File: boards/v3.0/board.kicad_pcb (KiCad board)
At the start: 2 copper layers, 65 parts, among them J2 KF301-2P, J3 KF301-2P, J4 KF301-2P, J5 KF301-2P, J6 KF301-2P, J7 KF301-2P, P1 Pin Header, P2 Pin Header, P3 Pin Header, P4 Pin Header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

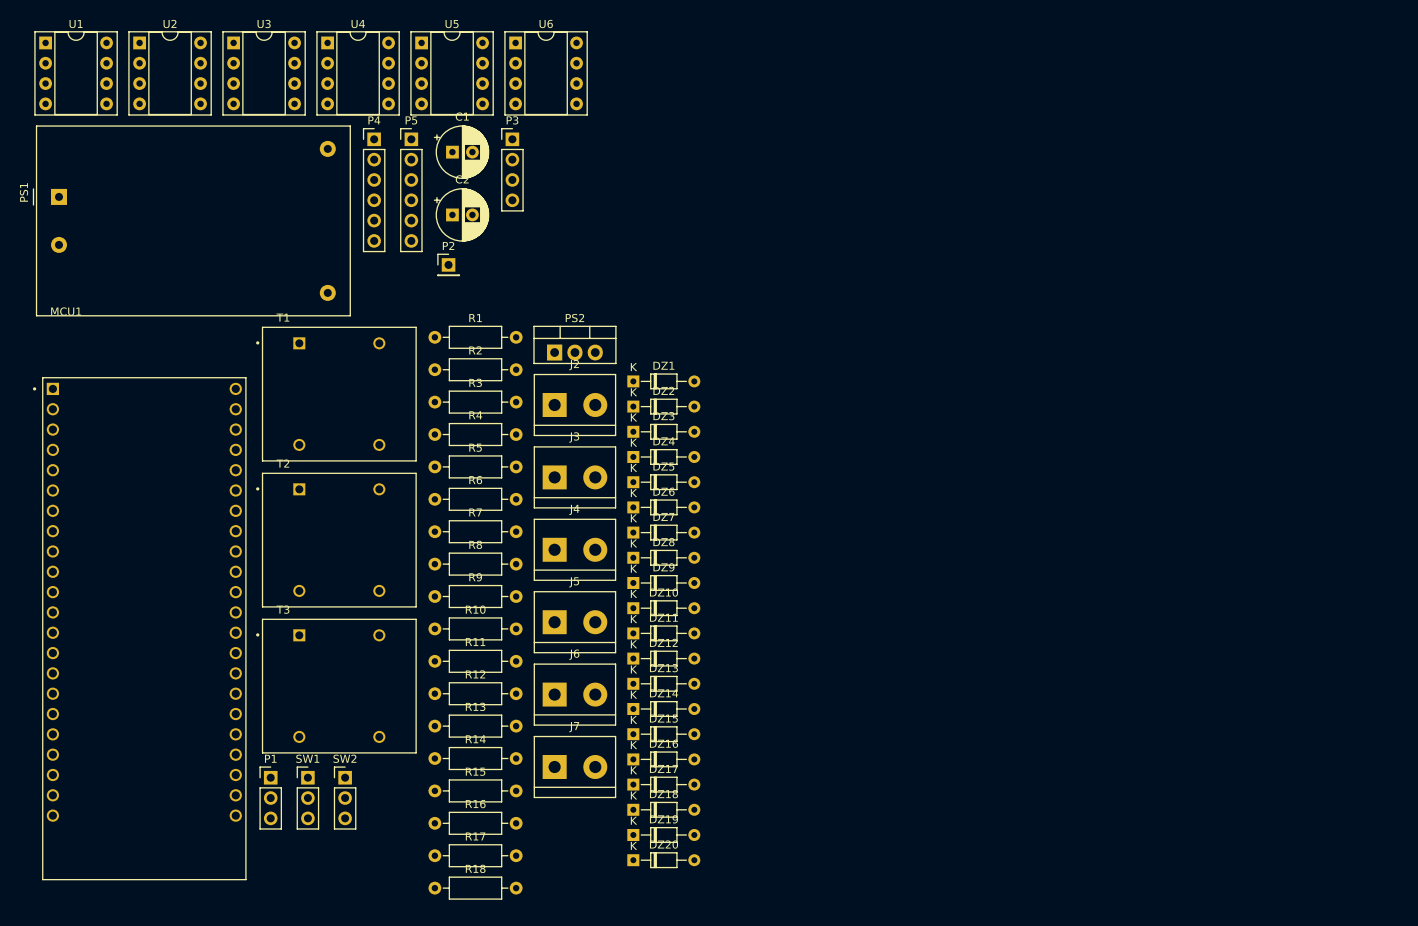
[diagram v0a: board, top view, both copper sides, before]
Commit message: Finish of board v3.0 development and code update
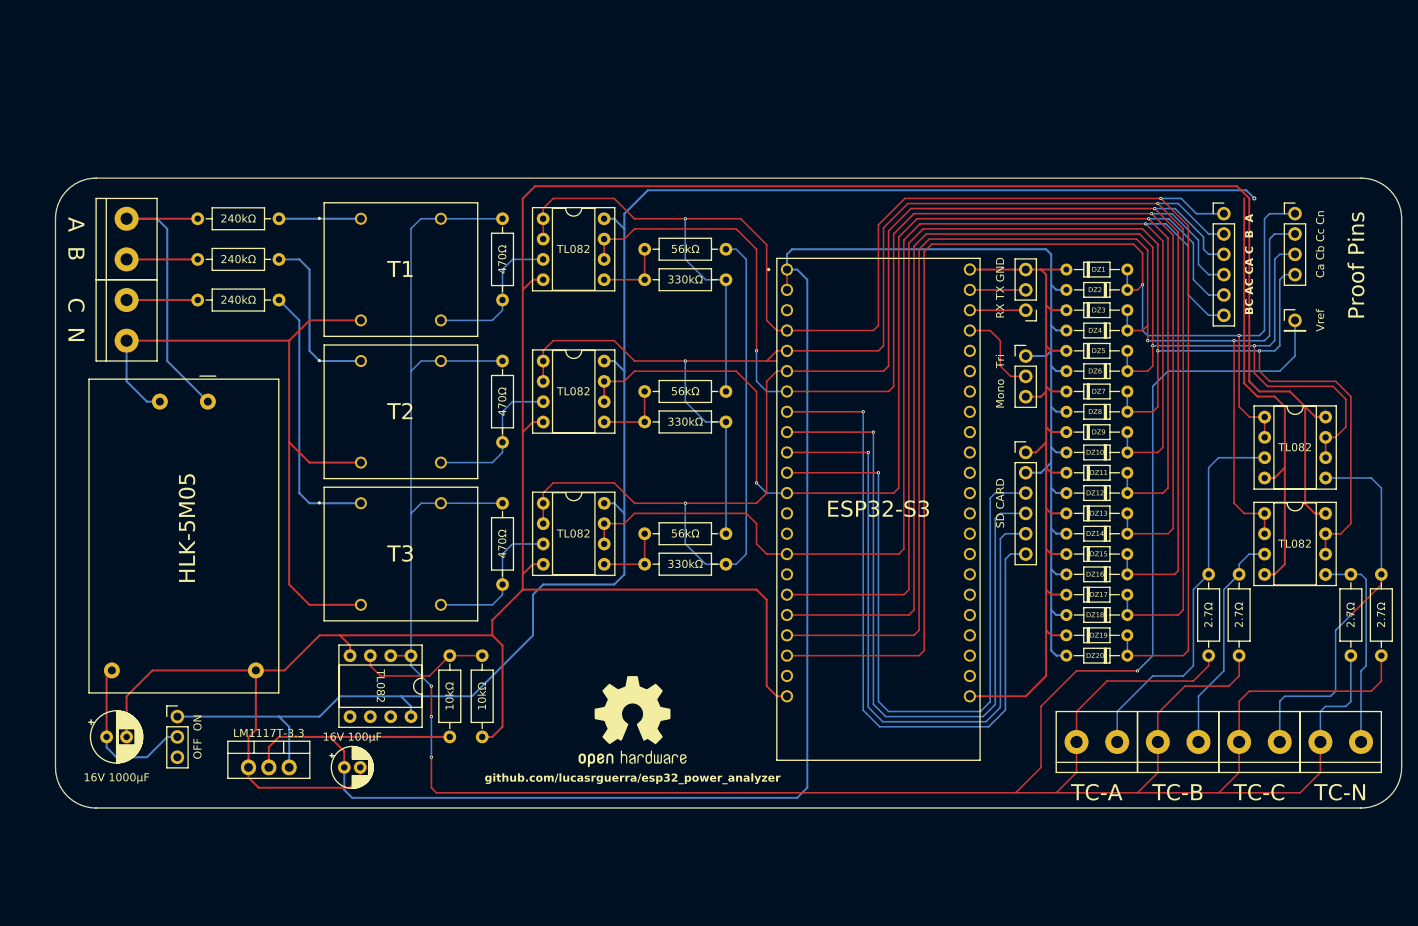
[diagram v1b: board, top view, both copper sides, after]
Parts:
- removed J7: KF301-2P, TerminalBlock:TerminalBlock_bornier-2_P5.08mm
- added G***: LOGO, LOGO, F.Cu at (135.6, 117.5)
- added J1: KF301-2P, TerminalBlock:TerminalBlock_bornier-2_P5.08mm, F.Cu at (72.4, 54.6)
- C2: value 25V 220µF -> 16V 100µF; footprint Capacitor_THT:CP_Radial_D6.3mm_P2.50mm -> Capacitor_THT:CP_Radial_D5.0mm_P2.00mm
- moved R17 123.4 mm to (229.2, 99.1), turned to -90 degrees
- moved R18 121.0 mm to (225.4, 99.1), turned to -90 degrees
- moved U5 115.3 mm to (214.7, 79.4)
- moved P1 111.0 mm to (184.8, 66.0), turned to 180 degrees
- moved U6 110.6 mm to (214.6, 91.5)
- moved P4 106.6 mm to (209.6, 54.0)
- moved P2 106.0 mm to (218.4, 67.3)
- moved R16 105.2 mm to (211.5, 99.1), turned to -90 degrees
- moved R15 100.4 mm to (207.6, 99.1), turned to -90 degrees
- moved SW2 100.1 mm to (184.8, 71.8)
- moved P3 98.3 mm to (218.4, 54.0)
- moved J6 95.9 mm to (221.6, 120.0)
- moved MCU1 93.0 mm to (166.4, 90.9)
- moved U1 89.2 mm to (107.9, 109.2), turned to -90 degrees
- moved J5 86.9 mm to (211.5, 120.0)
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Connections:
- C1 pad 1: Vin -> Power
- DZ1 pad 2: Treated Wave A -> Current A
- DZ10 pad 1: Treated Wave AB -> Treated Wave BC
- DZ11 pad 2: Treated Wave BC -> Treated Wave AB
- DZ12 pad 1: Treated Wave BC -> Treated Wave AB
- DZ13 pad 2: Current A -> Treated Wave CA
- DZ14 pad 1: Current A -> Treated Wave CA
- DZ15 pad 2: Current B -> Treated Wave C
- DZ16 pad 1: Current B -> Treated Wave C
- DZ17 pad 2: Current C -> Treated Wave B
- DZ18 pad 1: Current C -> Treated Wave B
- DZ19 pad 2: Current N -> Treated Wave A
- DZ2 pad 1: Treated Wave A -> Current A
- DZ20 pad 1: Current N -> Treated Wave A
- DZ3 pad 2: Treated Wave B -> Current B
- DZ4 pad 1: Treated Wave B -> Current B
- DZ5 pad 2: Treated Wave C -> Current C
- DZ6 pad 1: Treated Wave C -> Current C
- DZ7 pad 2: Treated Wave CA -> Current N
- DZ8 pad 1: Treated Wave CA -> Current N
- DZ9 pad 2: Treated Wave AB -> Treated Wave BC
- J3 pad 1: Line A -> TC A-2
- J3 pad 2: Line B -> TC A-1
- J4 pad 2: TC A-1 -> TC B-1
- J5 pad 2: TC B-1 -> TC C-1
- J6 pad 2: TC C-1 -> TC N-1
- P4 pad 1: Treated Wave C -> Treated Wave A
- P4 pad 3: Treated Wave A -> Treated Wave C
- P4 pad 4: Treated Wave BC -> Treated Wave CA
- P4 pad 6: Treated Wave CA -> Treated Wave BC
- PS1 pad 4: Vin -> Power
- PS2 pad 3: Net-(PS2-VI) -> Vin
- SW1 pad 1: Net-(PS2-VI) -> Vin
- SW1 pad 2: Vin -> Power
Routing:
- net GND: track 0.00 -> 464.5 mm
- net TC A-2: track 0.00 -> 417.1 mm, vias 0 -> 4
- net Vcc: track 0.00 -> 274.8 mm
- net Vin: track 0.00 -> 260.2 mm, vias 0 -> 1
- net Treated Wave C: track 0.00 -> 236.8 mm, vias 0 -> 2
- net Treated Wave A: track 0.00 -> 210.3 mm, vias 0 -> 2
- net Treated Wave B: track 0.00 -> 197.2 mm, vias 0 -> 2
- net Current N: track 0.00 -> 181.7 mm, vias 0 -> 2
- net Treated Wave AB: track 0.00 -> 175.3 mm, vias 0 -> 2
- net Treated Wave CA: track 0.00 -> 172.9 mm, vias 0 -> 2
- net Current B: track 0.00 -> 168.9 mm, vias 0 -> 2
- net Treated Wave BC: track 0.00 -> 168.2 mm, vias 0 -> 1
- net Current C: track 0.00 -> 167.3 mm, vias 0 -> 2
- net Current A: track 0.00 -> 158.8 mm, vias 0 -> 2
- net Neutral: track 0.00 -> 91.2 mm
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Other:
- board outline added: 168.3 x 78.7 mm
- board text added: "Proof Pins"
- board text added: "github.com/lucasrguerra/esp32_power_analyzer"

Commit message: Revision of the v3.0 board
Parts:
- moved J6 141.3 mm to (102.2, 44.5), turned to 180 degrees
- moved R18 129.1 mm to (102.2, 60.3), turned to 90 degrees
- moved J5 124.6 mm to (112.4, 44.5), turned to 180 degrees
- moved R17 123.1 mm to (112.4, 60.3), turned to 90 degrees
- moved J4 109.1 mm to (122.6, 44.5), turned to 180 degrees
- moved R16 97.0 mm to (122.6, 60.3), turned to 90 degrees
- moved J3 95.5 mm to (132.7, 44.5), turned to 180 degrees
- moved R15 84.3 mm to (132.7, 60.3), turned to 90 degrees
- moved DZ20 69.2 mm to (148.6, 60.3), turned to 90 degrees
- moved U5 67.7 mm to (160.0, 39.4), turned to -90 degrees
- moved DZ19 66.4 mm to (151.1, 52.7), turned to -90 degrees
- moved U6 64.2 mm to (177.2, 39.4), turned to -90 degrees
- moved DZ18 62.0 mm to (153.7, 60.3), turned to 90 degrees
- moved DZ17 59.4 mm to (156.2, 52.7), turned to -90 degrees
- moved DZ16 54.8 mm to (158.8, 60.3), turned to 90 degrees
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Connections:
- R15 pad 1: TC A-1 -> TC B-1
- R16 pad 1: TC B-1 -> TC C-1
- R17 pad 1: TC C-1 -> TC A-1
- U5 pad 1: Current A -> Current B
- U5 pad 2: Current A -> Current B
- U5 pad 3: TC A-1 -> TC B-1
- U6 pad 1: Current B -> Current A
- U6 pad 2: Current B -> Current A
- U6 pad 3: TC B-1 -> TC A-1
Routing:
- net TC A-2: track 417.1 -> 165.7 mm, vias 4 -> 0
- net TC N-1: track 25.9 -> 105.7 mm
- net Treated Wave A: track 210.3 -> 151.5 mm
- net Vin: track 260.2 -> 204.0 mm, vias 1 -> 0
- net GND: track 464.5 -> 411.8 mm, vias 0 -> 1
- net TC B-1: track 28.0 -> 79.2 mm
- net Treated Wave CA: track 172.9 -> 123.9 mm, vias 2 -> 1
- net Treated Wave AB: track 175.3 -> 129.5 mm, vias 2 -> 1
- net Treated Wave B: track 197.2 -> 157.3 mm, vias 2 -> 3
- net Treated Wave C: track 236.8 -> 202.6 mm, vias 2 -> 3
- net Treated Wave BC: track 168.2 -> 134.1 mm
- net TC A-1: track 48.8 -> 82.4 mm
- net Vcc: track 274.8 -> 307.6 mm, vias 0 -> 2
- net TC C-1: track 47.8 -> 76.5 mm, vias 1 -> 0
- net Current N: track 181.7 -> 156.0 mm
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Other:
- board size 168.3 x 78.7 mm -> 121.9 x 105.4 mm
- board text added: "Analisador de Qualidade de Energia"
- board text removed: "Proof Pins"

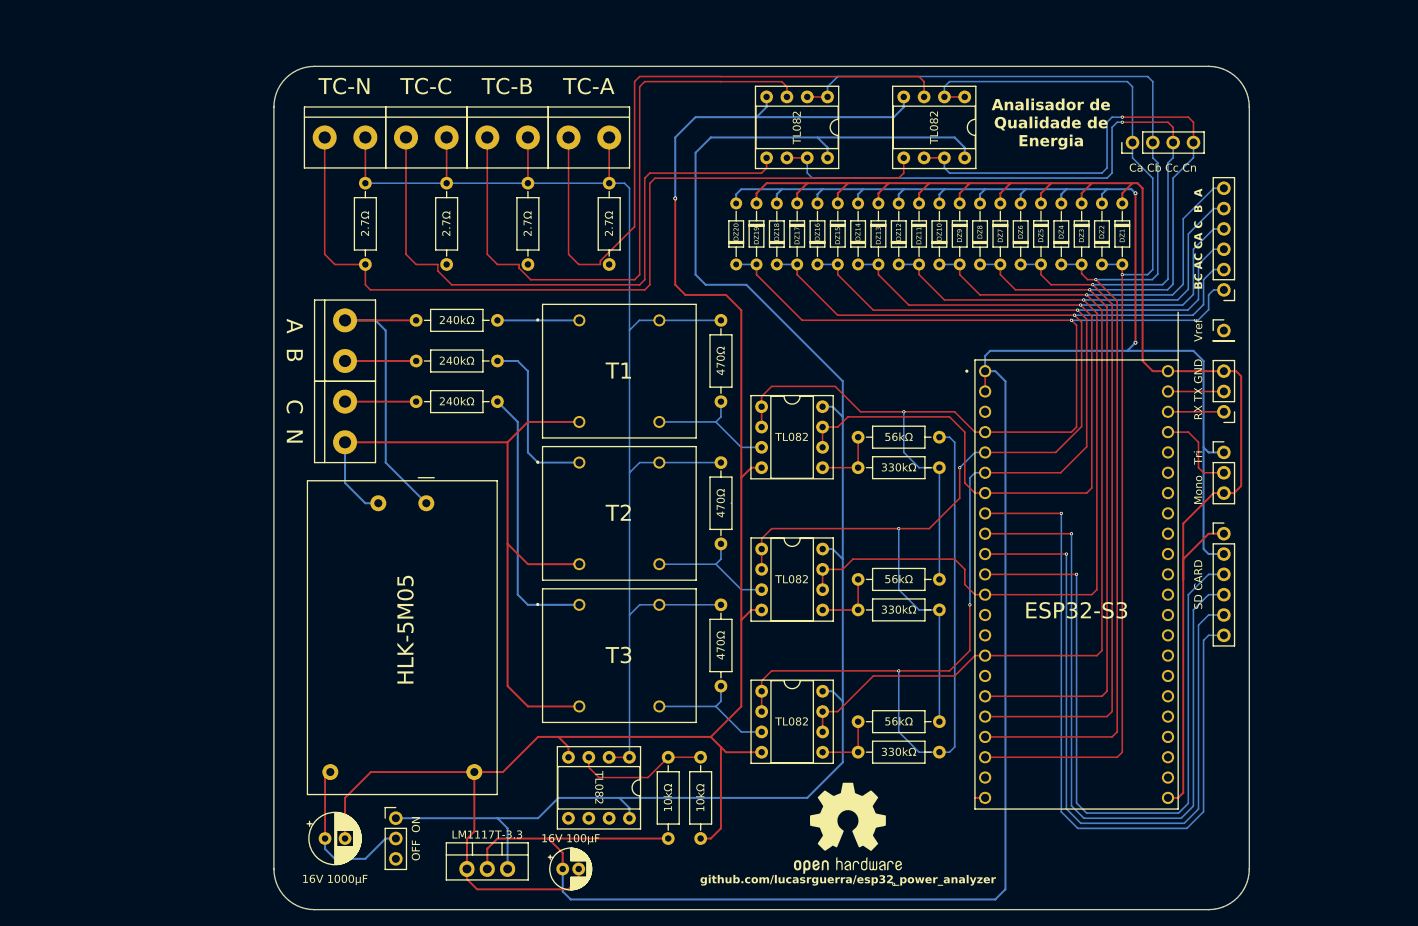
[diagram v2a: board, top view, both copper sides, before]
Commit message: Reduction in the size of v3.0 board
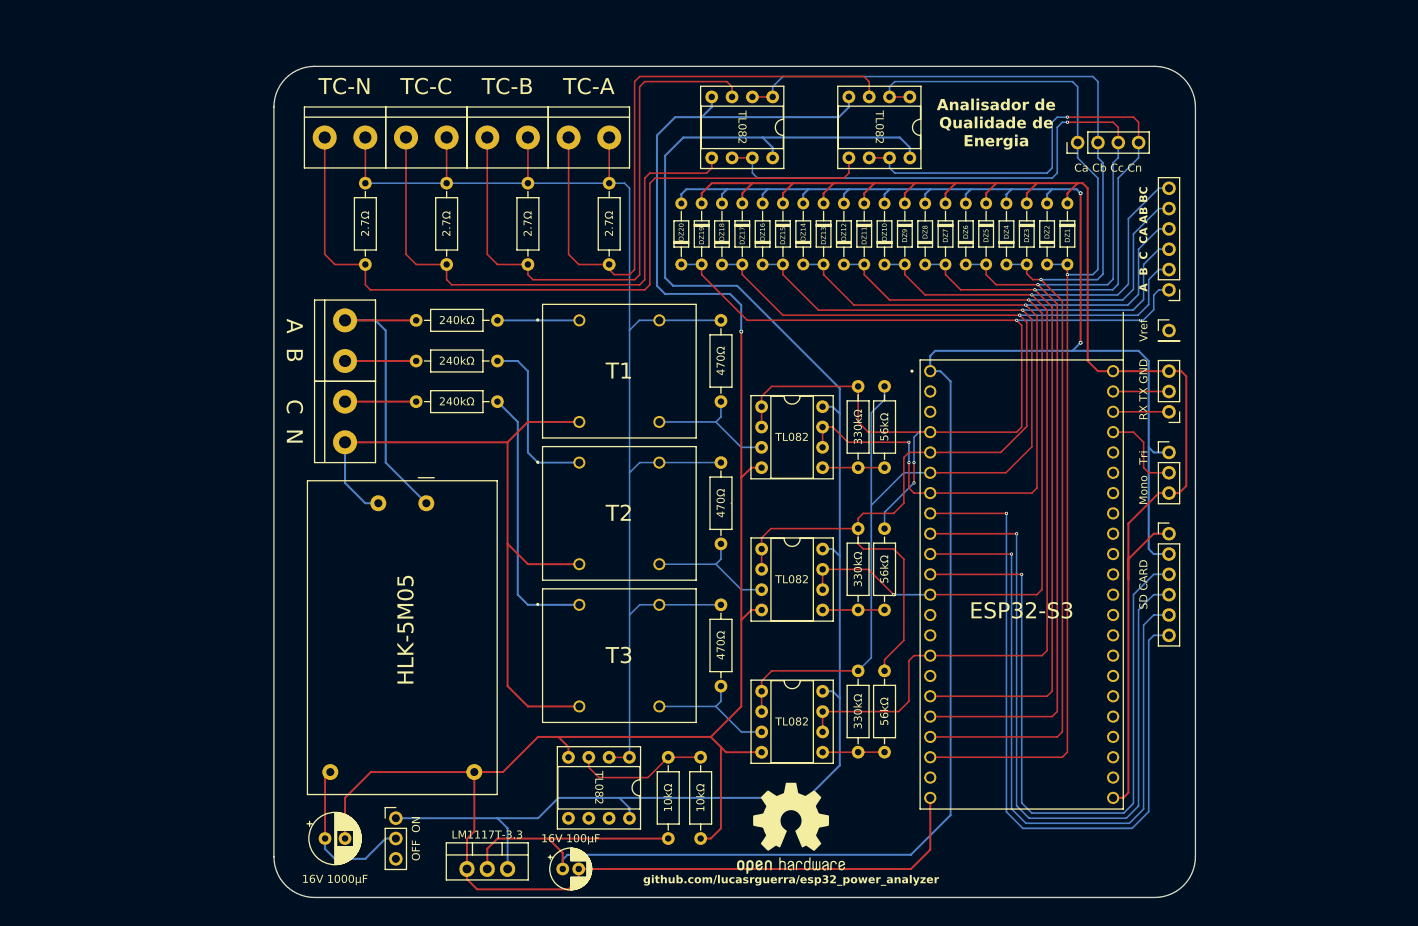
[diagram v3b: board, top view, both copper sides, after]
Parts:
- moved R17 20.3 mm to (132.7, 60.3)
- moved R11 14.4 mm to (163.8, 93.3), turned to -90 degrees
- moved R13 14.4 mm to (163.8, 111.1), turned to -90 degrees
- moved R9 14.4 mm to (163.8, 75.6), turned to -90 degrees
- moved R16 10.2 mm to (112.4, 60.3)
- moved R15 10.2 mm to (122.6, 60.3)
- moved R10 9.35 mm to (167.1, 75.6), turned to -90 degrees
- moved R12 9.35 mm to (167.1, 93.3), turned to -90 degrees
- moved R14 9.35 mm to (167.1, 111.1), turned to -90 degrees
- moved G*** 7.11 mm to (155.4, 130.8)
- moved DZ1 6.86 mm to (190.0, 52.7)
- moved DZ10 6.86 mm to (167.1, 60.3)
- moved DZ12 6.86 mm to (162.1, 60.3)
- moved DZ13 6.86 mm to (159.5, 52.7)
- moved DZ14 6.86 mm to (157.0, 60.3)
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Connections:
- MCU1 pad J1_2: Vcc -> unconnected-(MCU1-3V3__1-PadJ1_2)
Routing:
- net Treated Wave C: track 202.6 -> 153.6 mm, vias 3 -> 1
- net GND: track 411.8 -> 460.3 mm
- net Vcc: track 307.6 -> 288.7 mm
- net Treated Wave A: track 151.5 -> 138.2 mm, vias 2 -> 3
- net Treated Wave B: track 157.3 -> 148.0 mm, vias 3 -> 1
- net Treated Wave AB: track 129.5 -> 120.4 mm, vias 1 -> 2
- net Treated Wave CA: track 123.9 -> 115.6 mm, vias 1 -> 3
- net TC N-1: track 105.7 -> 98.8 mm
- net TC B-1: track 79.2 -> 72.8 mm
- net TC C-1: track 76.5 -> 70.3 mm
- net Treated Wave BC: track 134.1 -> 130.2 mm
- net TC A-1: track 82.4 -> 79.8 mm
- net Vin: track 204.0 -> 202.1 mm
- net Net-(U4B-+): track 8.25 -> 7.74 mm
- net Net-(U3B-+): track 8.25 -> 7.74 mm
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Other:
- board size 121.9 x 105.4 mm -> 115.2 x 103.9 mm

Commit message: Revision in the v3.0 board
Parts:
- moved G*** 90.7 mm to (180.6, 43.7)
- moved PS2 27.4 mm to (139.7, 124.1)
- moved C1 26.7 mm to (123.3, 126.4)
- moved SW1 26.3 mm to (131.4, 122.6)
- moved U1 24.1 mm to (159.4, 121.3)
- moved R1 23.8 mm to (163.8, 130.8)
- moved R2 23.0 mm to (167.1, 120.7)
- moved C2 16.3 mm to (141.7, 129.1), turned to 180 degrees
- moved R10 5.72 mm to (167.1, 69.8)
- moved R11 5.72 mm to (163.8, 87.6)
- moved R12 5.72 mm to (167.1, 87.6)
- moved R13 5.72 mm to (163.8, 105.4)
- moved R14 5.72 mm to (167.1, 105.4)
- moved R9 5.72 mm to (163.8, 69.8)
- moved U2 5.72 mm to (151.8, 72.4)
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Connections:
- MCU1 pad J1_12: Treated Wave AB -> Treated Wave C
- MCU1 pad J1_5: Treated Wave B -> Treated Wave CA
- MCU1 pad J1_6: Treated Wave C -> Treated Wave B
- MCU1 pad J1_7: Treated Wave CA -> Treated Wave AB
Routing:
- net GND: track 460.3 -> 385.7 mm
- net Vcc: track 288.7 -> 251.8 mm
- net TC A-2: track 165.7 -> 188.4 mm
- net Vin: track 202.1 -> 179.7 mm
- net Treated Wave C: track 153.6 -> 173.7 mm
- net Power: track 20.3 -> 38.7 mm
- net Treated Wave AB: track 120.4 -> 108.4 mm, vias 2 -> 3
- net Treated Wave A: track 138.2 -> 142.6 mm, vias 3 -> 1
- net Treated Wave BC: track 130.2 -> 127.2 mm
- net Treated Wave CA: track 115.6 -> 113.2 mm
- net Wave B: track 16.9 -> 15.0 mm
- net Wave A: track 16.9 -> 14.9 mm
- net Wave C: track 16.9 -> 15.0 mm
- net Current N: track 156.0 -> 157.7 mm
- net Treated Wave B: track 148.0 -> 146.9 mm
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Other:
- board size 115.2 x 103.9 mm -> 113.3 x 98 mm
- board text removed: "Analisador de Qualidade de Energia"
